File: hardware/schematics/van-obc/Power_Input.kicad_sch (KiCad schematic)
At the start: 11 parts, among them J10 J_LOADS, Q1 IRF4905, U1 LM2596 Module, U2 MP2307

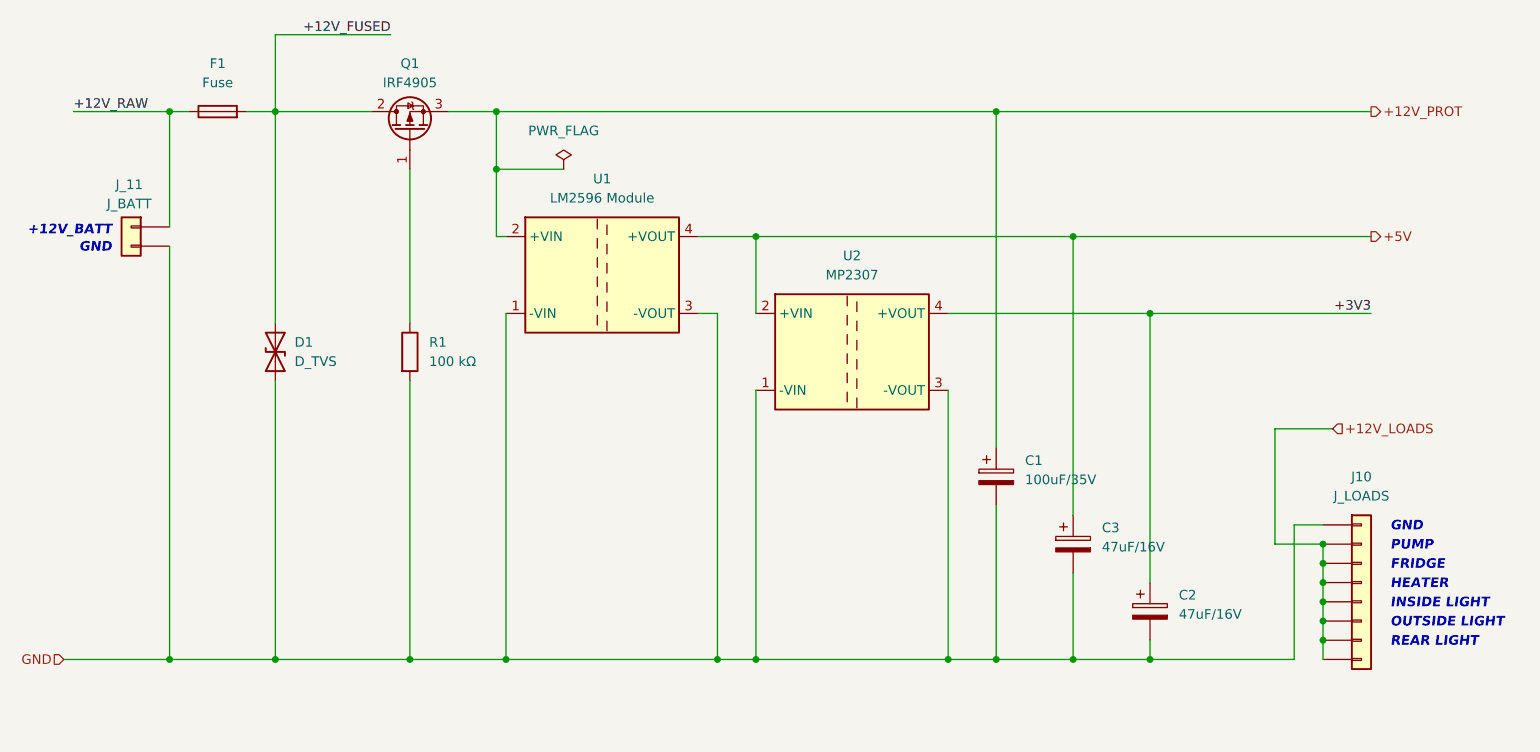
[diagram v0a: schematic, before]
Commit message: fix(tests): Corrections majeures KY040, BME280, MPU6050
- KY040 v2.1.0: Fix comptage + anti-rebond capacitif
- BME280 v1.0.1: Fix begin() avec &Wire
- MPU6050 v2.0.0: Simplification (acc only, dérive <2°)
- Ajout diagnostic_bme280.ino + CHANGELOG

Tests: 6/11 validés (55%)
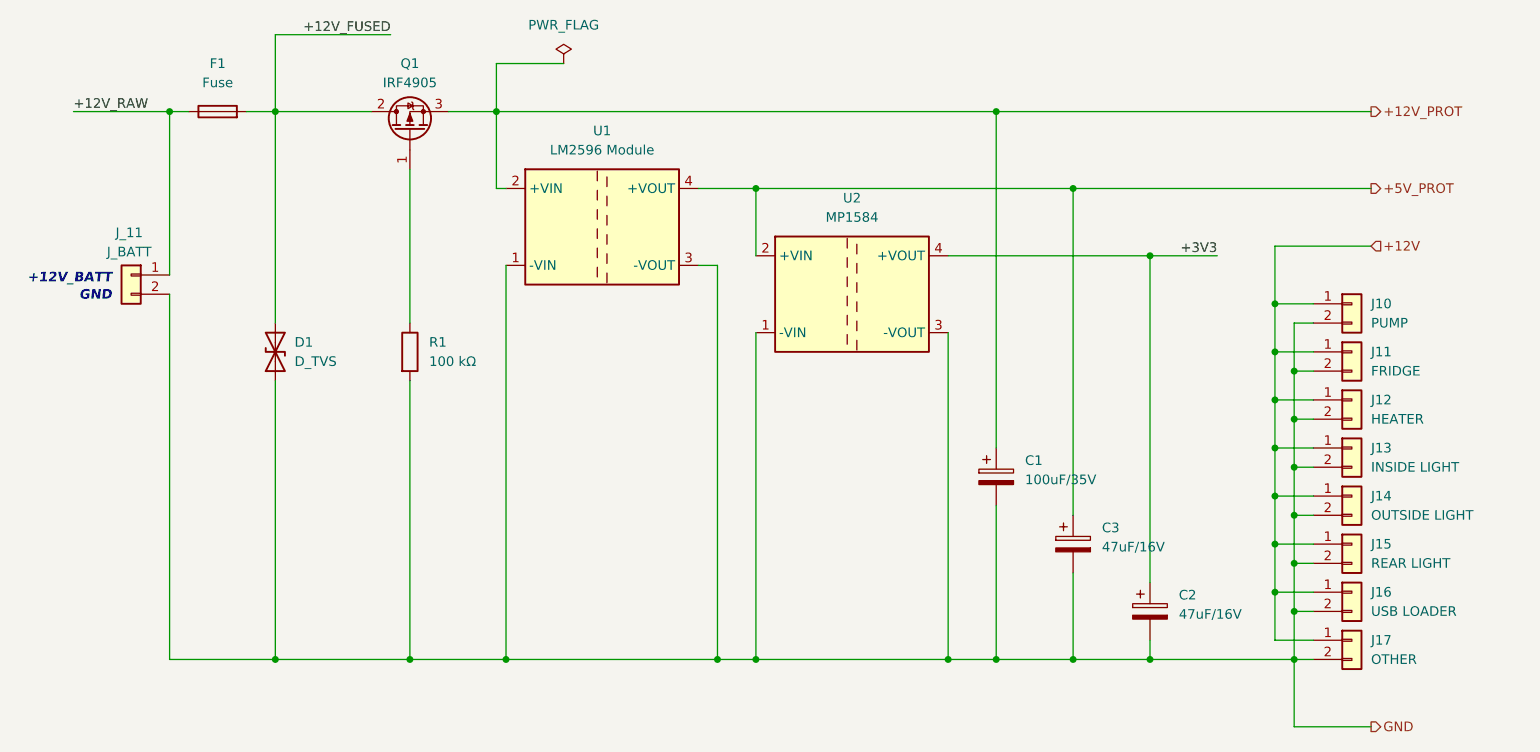
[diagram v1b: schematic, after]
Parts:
- removed J10: J_LOADS, symbol Connector_Generic:Conn_01x08
- added J10: PUMP, MyModules:Connecteur 2 vis, symbol Connector_Generic:Conn_01x02
- added J11: FRIDGE, MyModules:Connecteur 2 vis, symbol Connector_Generic:Conn_01x02
- added J12: HEATER, MyModules:Connecteur 2 vis, symbol Connector_Generic:Conn_01x02
- added J13: INSIDE LIGHT, MyModules:Connecteur 2 vis, symbol Connector_Generic:Conn_01x02
- added J14: OUTSIDE LIGHT, MyModules:Connecteur 2 vis, symbol Connector_Generic:Conn_01x02
- added J15: REAR LIGHT, MyModules:Connecteur 2 vis, symbol Connector_Generic:Conn_01x02
- added J16: USB LOADER, MyModules:Connecteur 2 vis, symbol Connector_Generic:Conn_01x02
- added J17: OTHER, MyModules:Connecteur 2 vis, symbol Connector_Generic:Conn_01x02
- C1: footprint (none) -> Capacitor_THT:CP_Radial_D8.0mm_P3.50mm
- C2, C3: footprint (none) -> Capacitor_THT:CP_Radial_D6.3mm_P2.50mm
- D1: footprint (none) -> Diode_SMD:D_SMA-SMB_Universal_Handsoldering
- F1: footprint (none) -> Fuse:Fuseholder_Clip-5x20mm_Bel_FC-203-22_Lateral_P17.80x5.00mm_D1.17mm_Horizontal
- J_11: footprint (none) -> MyModules:Connecteur 2 vis
- R1: footprint (none) -> Resistor_THT:R_Axial_DIN0207_L6.3mm_D2.5mm_P10.16mm_Horizontal
- U1: footprint Converter_DCDC:Converter_DCDC_Murata_CRE1xxxxxxSC_THT -> MyModules:LM2596_Breakout
- U2: value MP2307 -> MP1584; footprint Converter_DCDC:Converter_DCDC_Murata_CRE1xxxxxxSC_THT -> MyModules:MP1584_Breakout
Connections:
- net GND: now also J10.2 (Pin_2), J11.2 (Pin_2), J12.2 (Pin_2), J13.2 (Pin_2), J14.2 (Pin_2), J15.2 (Pin_2), J16.2 (Pin_2), J17.2 (Pin_2)
- net +5V renamed +5V_PROT
- new net +12V: J10.1 (Pin_1), J11.1 (Pin_1), J12.1 (Pin_1), J13.1 (Pin_1), J14.1 (Pin_1), J15.1 (Pin_1), J16.1 (Pin_1), J17.1 (Pin_1)
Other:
- note removed: "FRIDGE"
- note removed: "HEATER"
- note removed: "INSIDE LIGHT"
- note removed: "OUTSIDE LIGHT"
- note removed: "PUMP"
- note removed: "REAR LIGHT"
- moved on the sheet: U1, U2
